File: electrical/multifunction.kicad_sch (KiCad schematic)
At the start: 30 parts

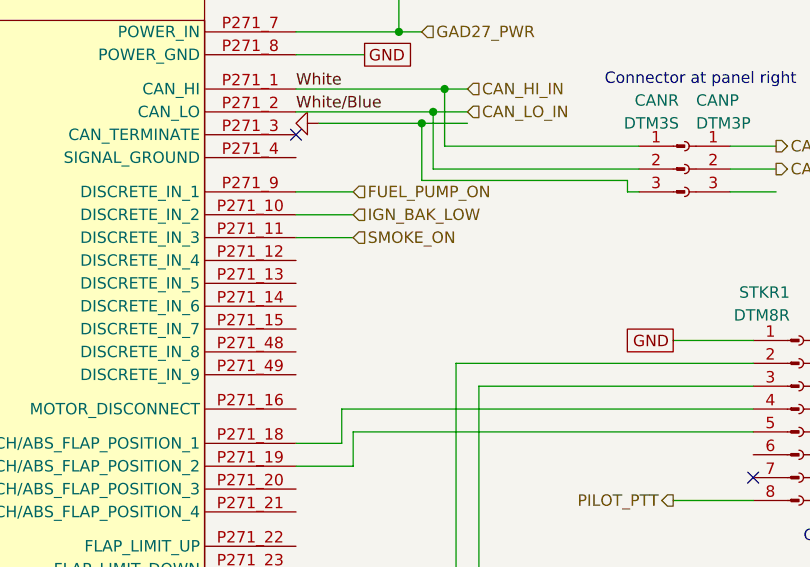
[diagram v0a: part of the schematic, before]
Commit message: Placed active high discretes for GAD 27 to pins 8 & 9.
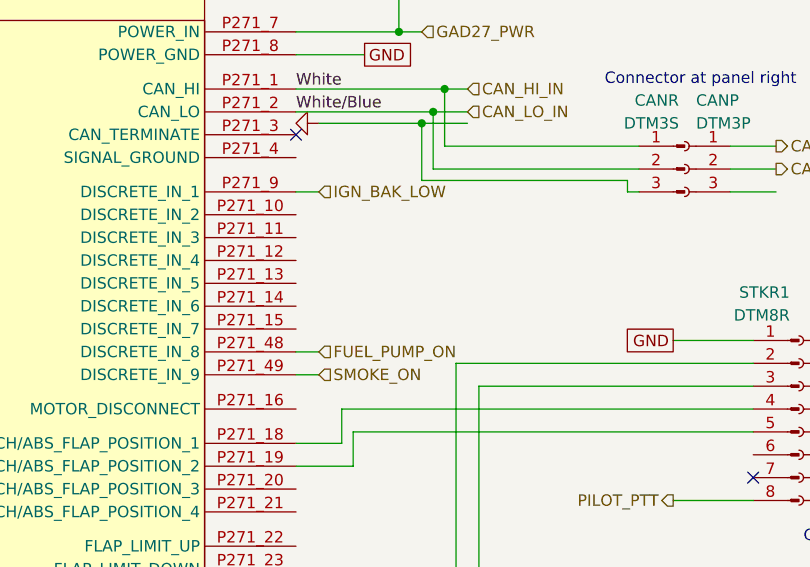
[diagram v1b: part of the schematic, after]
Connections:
- net FUEL_PUMP_ON: now also GAD27.P271_48 (DISCRETE_IN_8); no longer GAD27.P271_9 (DISCRETE_IN_1)
- net IGN_BAK_LOW: now also GAD27.P271_9 (DISCRETE_IN_1); no longer GAD27.P271_10 (DISCRETE_IN_2)
- net SMOKE_ON: now also GAD27.P271_49 (DISCRETE_IN_9); no longer GAD27.P271_11 (DISCRETE_IN_3)
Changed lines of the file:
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@@
 	(title_block
 		(title "Flaps, Lights & Trim")
-		(date "2026-01-01")
-		(rev "1.2.3")
+		(date "2026-01-08")
+		(rev "1.2.6")
 		(company "N877RV")
 	)
@@
 	(wire
 		(pts
+			(xy 81.28 64.77) (xy 83.82 64.77)
+		)
+		(stroke
+			(width 0)
+			(type default)
+		)
+	)
+	(wire
+		(pts
 			(xy 111.76 148.59) (xy 111.76 158.75)
 		)
@@
 	(wire
 		(pts
-			(xy 81.28 49.53) (xy 87.63 49.53)
-		)
-		(stroke
-			(width 0)
-			(type default)
-		)
-	)
-	(wire
-		(pts
 			(xy 135.89 161.29) (xy 110.49 161.29)
 		)
@@
 	(wire
 		(pts
+			(xy 81.28 62.23) (xy 83.82 62.23)
+		)
+		(stroke
+			(width 0)
+			(type default)
+		)
+	)
+	(wire
+		(pts
 			(xy 101.6 66.04) (xy 132.08 66.04)
 		)
@@
 	(wire
 		(pts
+			(xy 81.28 44.45) (xy 83.82 44.45)
+		)
+		(stroke
+			(width 0)
+			(type default)
+		)
+	)
+	(wire
+		(pts
 			(xy 87.63 74.93) (xy 87.63 71.12)
 		)
@@
 	(wire
 		(pts
-			(xy 81.28 46.99) (xy 87.63 46.99)
-		)
-		(stroke
-			(width 0)
-			(type default)
-		)
-	)
-	(wire
-		(pts
 			(xy 81.28 33.02) (xy 97.79 33.02)
 		)
@@
 			(width 0)
 			(type dash)
-		)
-	)
-	(wire
-		(pts
-			(xy 81.28 44.45) (xy 87.63 44.45)
-		)
-		(stroke
-			(width 0)
-			(type default)
 		)
 	)
@@
 	(hierarchical_label "SMOKE_ON"
 		(shape input)
-		(at 87.63 49.53 0)
+		(at 83.82 64.77 0)
 		(effects
 			(font
@@
 	(hierarchical_label "IGN_BAK_LOW"
 		(shape input)
-		(at 87.63 46.99 0)
+		(at 83.82 44.45 0)
 		(effects
 			(font
@@
 	(hierarchical_label "FUEL_PUMP_ON"
 		(shape input)
-		(at 87.63 44.45 0)
-		(effects
-			(font
+		(at 83.82 62.23 0)
+		(effects
+			(font

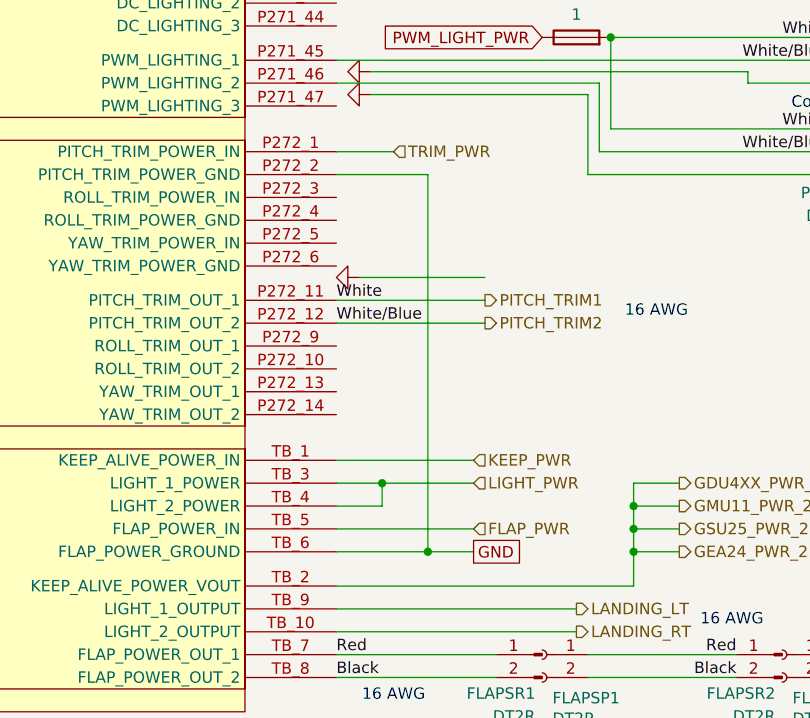
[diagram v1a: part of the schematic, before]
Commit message: Fixed can hi pin on GTR 20. Changed how ACX-BT wires with low vs. shield. Added pitch trim colors. Removed pitch trim ground going to flaps ground. Removed extra connector on GDL 52 and changed to 4 wire shielded instead of two 2 wire shielded.
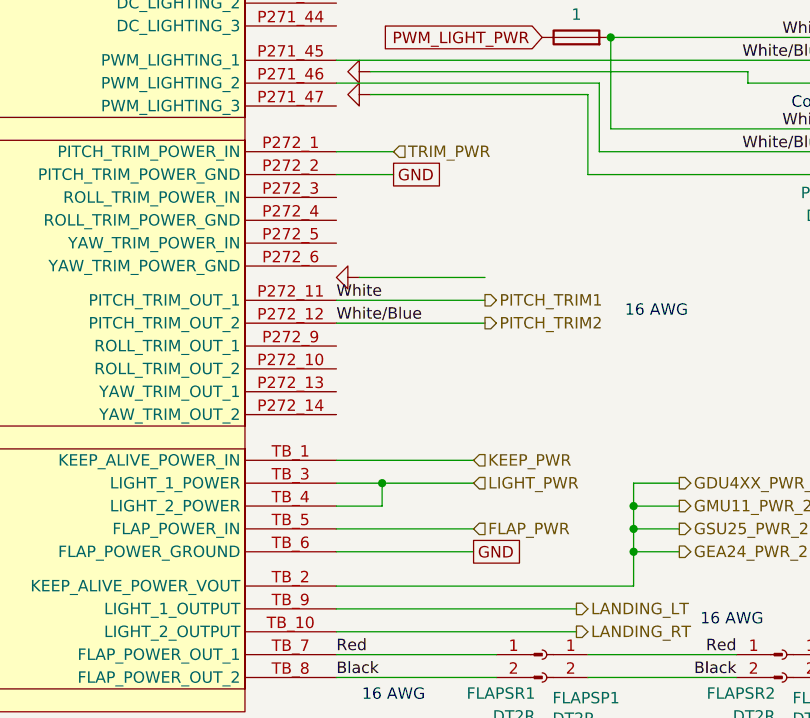
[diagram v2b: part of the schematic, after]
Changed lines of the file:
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@@
 	(title_block
 		(title "Flaps, Lights & Trim")
-		(date "2026-01-08")
-		(rev "1.2.6")
+		(date "2026-01-13")
+		(rev "1.2.11")
 		(company "N877RV")
 	)
@@
 	)
 	(junction
-		(at 91.44 205.74)
-		(diameter 0)
-		(color 0 0 0 0)
-	)
-	(junction
 		(at 189.23 66.04)
 		(diameter 0)
@@
 	(wire
 		(pts
-			(xy 81.28 163.83) (xy 91.44 163.83)
+			(xy 81.28 163.83) (xy 87.63 163.83)
 		)
 		(stroke
@@
 	(wire
 		(pts
-			(xy 81.28 205.74) (xy 91.44 205.74)
+			(xy 81.28 205.74) (xy 96.52 205.74)
 		)
 		(stroke
@@
 	(wire
 		(pts
-			(xy 91.44 163.83) (xy 91.44 205.74)
-		)
-		(stroke
-			(width 0)
-			(type default)
-		)
-	)
-	(wire
-		(pts
 			(xy 99.06 63.5) (xy 99.06 90.17)
 		)
@@
 		(pts
 			(xy 185.42 63.5) (xy 189.23 63.5)
-		)
-		(stroke
-			(width 0)
-			(type default)
-		)
-	)
-	(wire
-		(pts
-			(xy 91.44 205.74) (xy 96.52 205.74)
 		)
 		(stroke
@@
 		)
 	)
+	(global_label "GND"
+		(shape passive)
+		(at 87.63 163.83 0)
+		(fields_autoplaced yes)
+		(effects
+			(font
+				(size 1.27 1.27)
+			)
+			(justify left)
+		)
+		(property "Intersheetrefs" "${INTERSHEET_REFS}"
+			(at 93.3744 163.83 0)
+			(effects
+				(font
+					(size 1.27 1.27)
+				)
+				(justify left)
+				(hide yes)
+			)
+		)
+	)

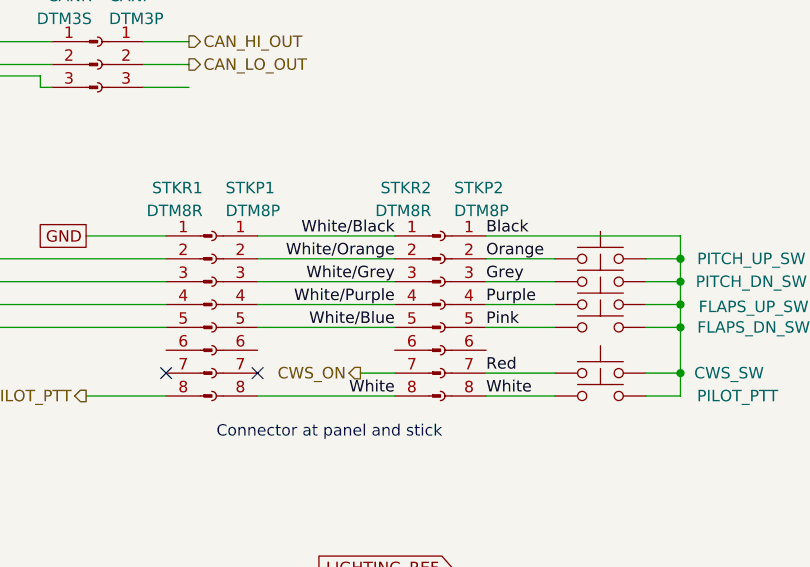
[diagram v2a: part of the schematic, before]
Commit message: Split Pitch Trim POS to go straight into connector. Changed colors on CO monitor to match what cable had. Changed colors of stick after father changed buttons.
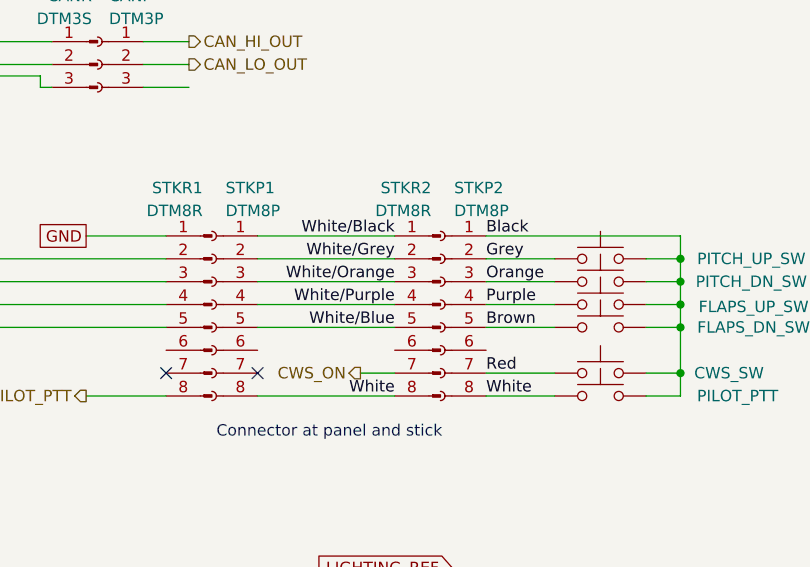
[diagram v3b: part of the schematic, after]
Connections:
- net Grey: now also PITCH_UP_SW.1, STKP2.2 (Pin_2); no longer PITCH_DN_SW.1, STKP2.3 (Pin_3)
- net Orange: now also PITCH_DN_SW.1, STKP2.3 (Pin_3); no longer PITCH_UP_SW.1, STKP2.2 (Pin_2)
- net White/Grey: now also STKP1.2 (Pin_2), STKR2.2 (Pin_2); no longer STKP1.3 (Pin_3), STKR2.3 (Pin_3)
- net White/Orange: now also STKP1.3 (Pin_3), STKR2.3 (Pin_3); no longer STKP1.2 (Pin_2), STKR2.2 (Pin_2)
- net Pink renamed Brown
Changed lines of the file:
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@@
 	(title_block
 		(title "Flaps, Lights & Trim")
-		(date "2026-01-13")
-		(rev "1.2.11")
+		(date "2026-01-15")
+		(rev "1.2.12")
 		(company "N877RV")
 	)
@@
 		)
 	)
-	(label "White{slash}Grey"
+	(label "White{slash}Orange"
 		(at 157.48 66.04 180)
 		(effects
@@
 		)
 	)
-	(label "Pink"
+	(label "Brown"
 		(at 167.64 71.12 0)
 		(effects
@@
 		)
 	)
-	(label "Grey"
+	(label "Orange"
 		(at 167.64 66.04 0)
 		(effects
@@
 		)
 	)
-	(label "Orange"
+	(label "Grey"
 		(at 167.64 63.5 0)
 		(effects
@@
 		)
 	)
-	(label "White{slash}Orange"
+	(label "White{slash}Grey"
 		(at 157.48 63.5 180)
 		(effects

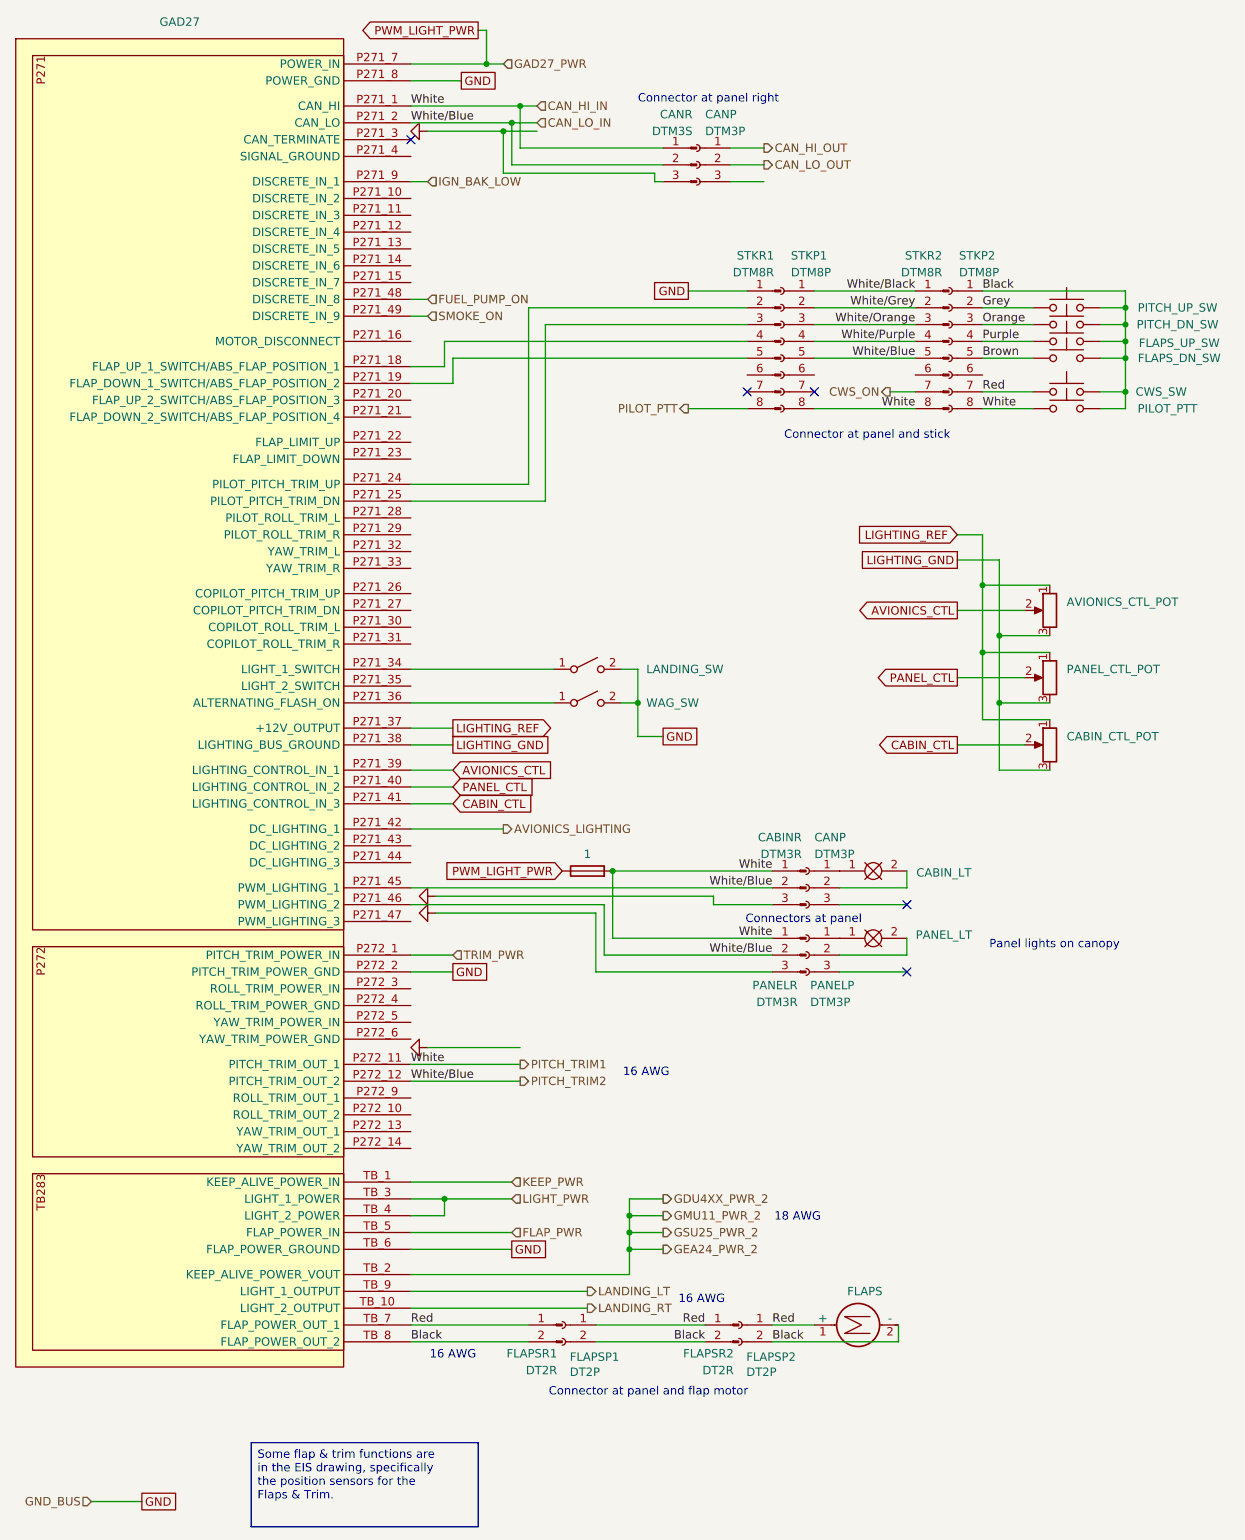
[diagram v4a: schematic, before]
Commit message: Wires light switch 2 discrete input into the same landing light switch
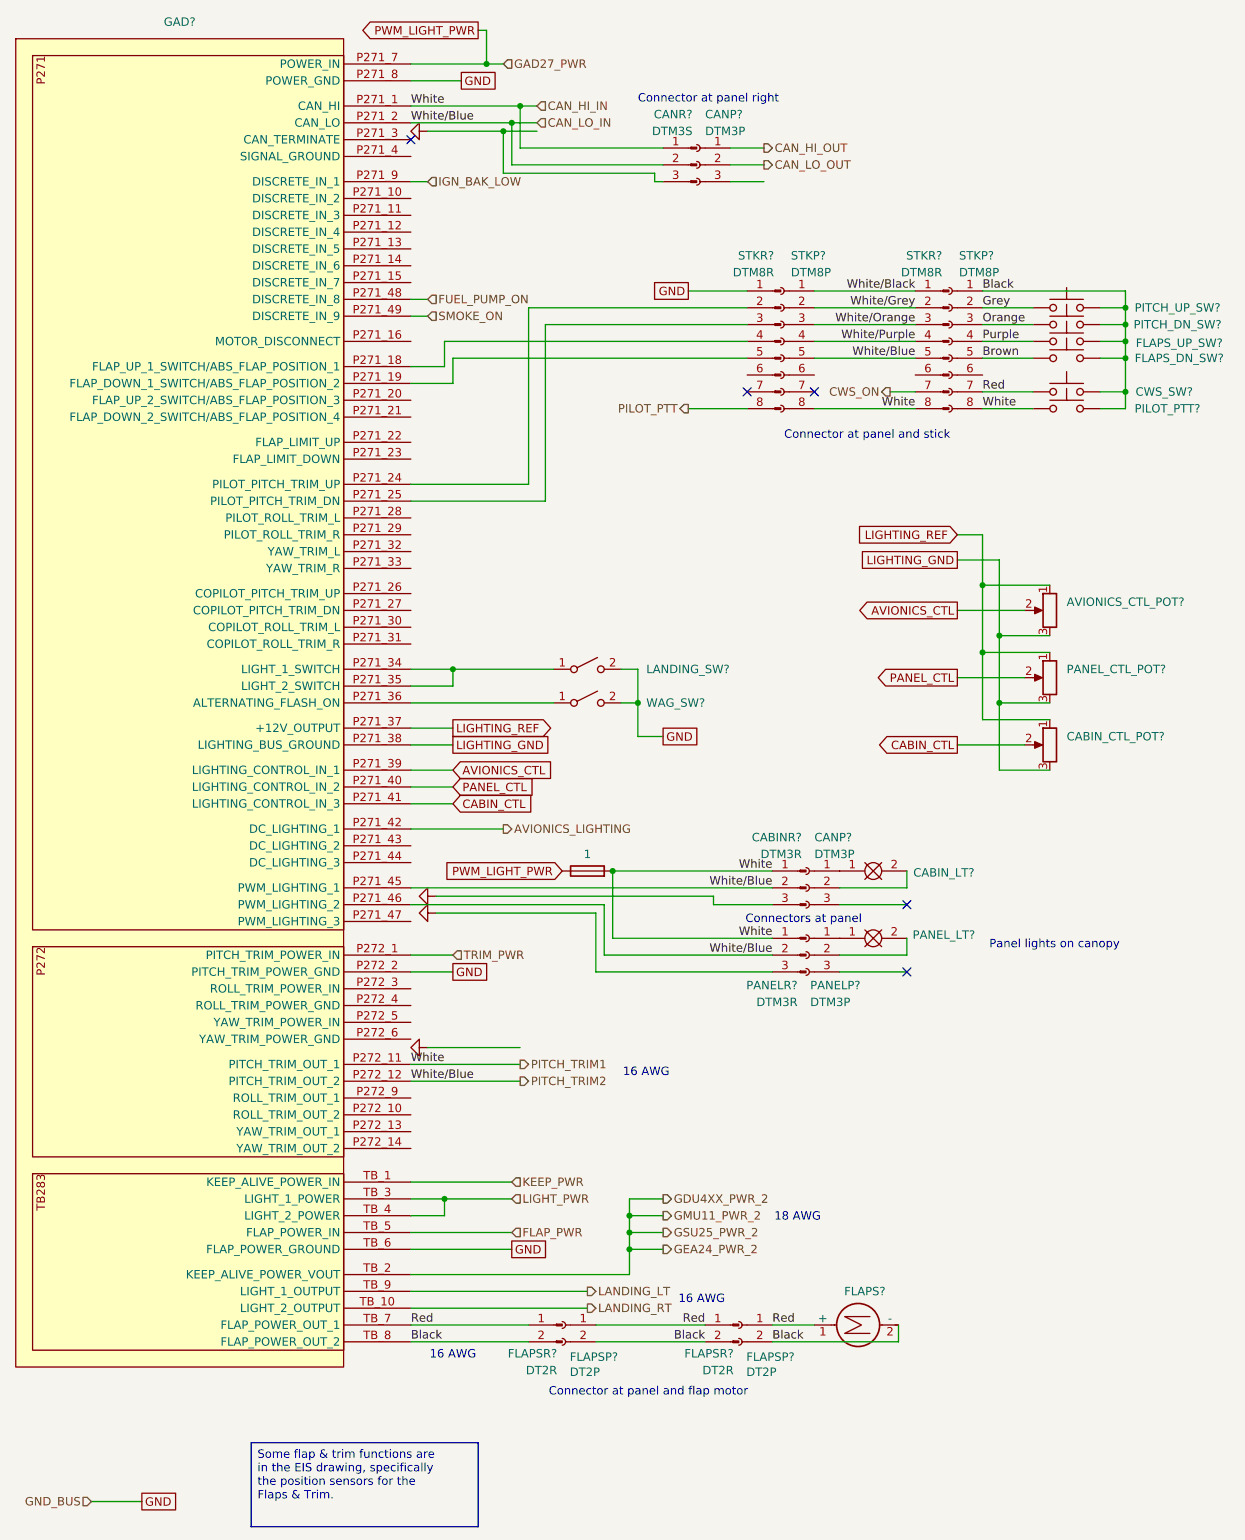
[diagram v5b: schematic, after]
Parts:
- renumbered AVIONICS_CTL_POT to AVIONICS_CTL_POT?, CABINR to CABINR?, CABIN_CTL_POT to CABIN_CTL_POT?, CABIN_LT to CABIN_LT?, CANP to CANP?, CANR to CANR?, CWS_SW to CWS_SW?, FLAPS to FLAPS?, FLAPSP1 to FLAPSP?, FLAPSP2 to FLAPSP?, FLAPSR2 to FLAPSR?, FLAPSR1 to FLAPSR?, FLAPS_DN_SW to FLAPS_DN_SW?, FLAPS_UP_SW to FLAPS_UP_SW?, GAD27 to GAD?, LANDING_SW to LANDING_SW?, PANELP to PANELP?, PANELR to PANELR?, PANEL_CTL_POT to PANEL_CTL_POT?, PANEL_LT to PANEL_LT?, PANEL_LT_FS to PANEL_LT_FS?, PILOT_PTT to PILOT_PTT?, PITCH_DN_SW to PITCH_DN_SW?, PITCH_UP_SW to PITCH_UP_SW?, STKP1 to STKP?, STKP2 to STKP?, STKR1 to STKR?, STKR2 to STKR?, WAG_SW to WAG_SW?
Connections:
- net at GAD?.P271_34 (LIGHT_1_SWITCH), LANDING_SW?.1 (A): now also GAD?.P271_35 (LIGHT_2_SWITCH)
